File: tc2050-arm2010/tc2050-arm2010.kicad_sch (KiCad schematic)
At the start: 7 parts, among them J1 Conn_02x05_Odd_Even, J2 Conn_02x10_Odd_Even, J3 Conn_ARM_JTAG_SWD_10, J4 Conn_ARM_JTAG_SWD_10, J5 Conn_02x03_Odd_Even, J6 Conn_01x07_Female

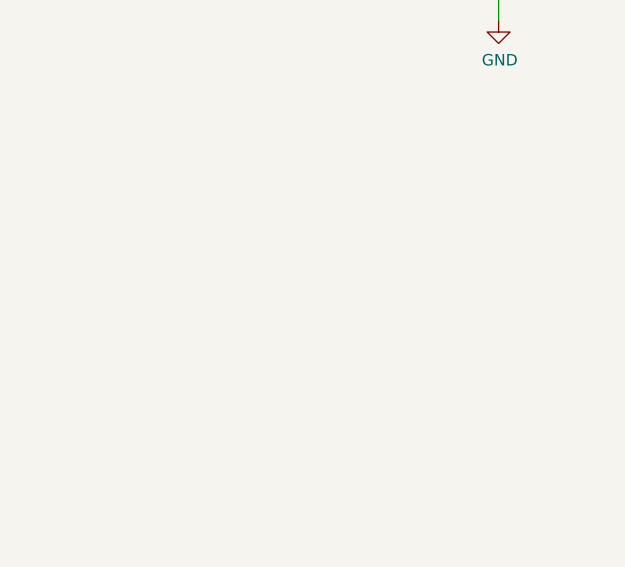
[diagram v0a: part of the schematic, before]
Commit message: Trap for young players: gnd disconnected on host ARM10 when STM32 part cut off
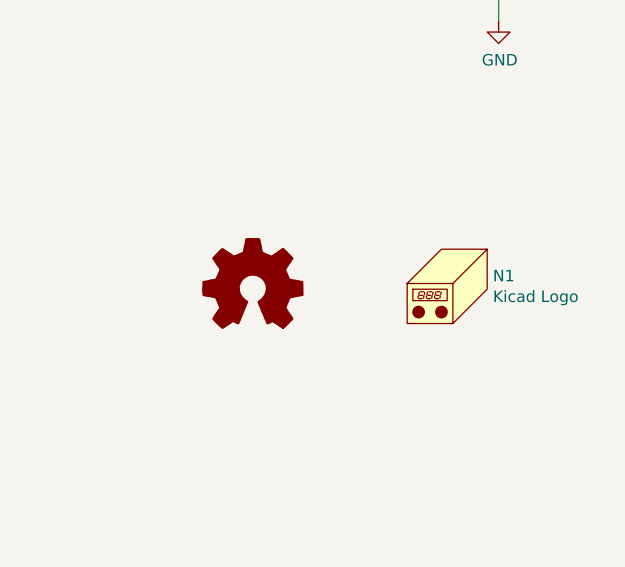
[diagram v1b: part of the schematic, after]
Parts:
- added LOGO1: Logo_Open_Hardware_Small, Symbol:OSHW-Logo2_7.3x6mm_SilkScreen, symbol Graphic:Logo_Open_Hardware_Small
- added N1: Kicad Logo, Symbol:KiCad-Logo2_5mm_SilkScreen, symbol Mechanical:Housing
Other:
- company: (none) -> It's only Audio
- title: (none) -> Universal ARM Debugger Connector
